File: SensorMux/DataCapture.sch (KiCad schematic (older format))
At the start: 0 parts

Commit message: Added byte start pulse generator
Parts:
- added C?: 220pF, symbol C
- added C?: C, symbol C
- added R?: 100, symbol R
- added R? (x2): 270, symbol R
- added U?: 74HC165, symbol 74LS165
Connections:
- new net: C?.2, R?.1
- new net: R?.1, U?.1 (Pl)
- new net +5V: C?.1, R?.1, U?.16 (VCC)
- new net CLK: U?.2 (CP)
- new net CLK_CNT_BIT_2: R?.2
- new net GND: C?.2, U?.15 (CE), U?.8 (GND)
- new net MISO: U?.9 (Q7)
- new net ~BYTE_START_PULSE: C?.1, R?.2, R?.2
- no-connect marks 0 -> 1
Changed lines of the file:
@@
 LIBS:contrib
 LIBS:valves
+LIBS:Trainiot
 LIBS:SensorMux-cache
 EELAYER 25 0
@@
 Comment4 ""
 $EndDescr
+Text HLabel 1350 4650 0    60   Input ~ 0
+CLK
+Wire Wire Line
+	1350 4650 8300 4650
+Text HLabel 1350 5900 0    60   Input ~ 0
+CLK_CNT_BUS
+Wire Bus Line
+	1350 5900 1850 5900
+Entry Wire Line
+	1550 5900 1650 6000
+Text Label 1700 6000 0    60   ~ 0
+CLK_CNT_BIT_2
+$Comp
+L C C?
+U 1 1 5A4D470C
+P 3250 6000
+F 0 "C?" H 3275 6100 50  0000 L CNN
+F 1 "220pF" H 3275 5900 50  0000 L CNN
+F 2 "" H 3288 5850 50  0001 C CNN
+F 3 "" H 3250 6000 50  0001 C CNN
+	1    3250 6000
+	0    1    1    0
+$EndComp
+Wire Wire Line
+	1650 6000 2650 6000
+$Comp
+L R R?
+U 1 1 5A4D4BAF
+P 2800 6000
+F 0 "R?" V 2880 6000 50  0000 C CNN
+F 1 "100" V 2800 6000 50  0000 C CNN
+F 2 "" V 2730 6000 50  0001 C CNN
+F 3 "" H 2800 6000 50  0001 C CNN
+	1    2800 6000
+	0    1    1    0
+$EndComp
+Wire Wire Line
+	3100 6000 2950 6000
+$Comp
+L R R?
+U 1 1 5A4D4C94
+P 3550 5600
+F 0 "R?" V 3630 5600 50  0000 C CNN
+F 1 "270" V 3550 5600 50  0000 C CNN
+F 2 "" V 3480 5600 50  0001 C CNN
+F 3 "" H 3550 5600 50  0001 C CNN
+	1    3550 5600
+	1    0    0    -1
+$EndComp
+Connection ~ 3550 6000
+Wire Wire Line
+	3550 6000 3550 5750
+Wire Wire Line
+	3550 5100 3550 5450
+Text Label 3850 6000 0    60   ~ 0
+~BYTE_START_PULSE
+$Comp
+L 74LS165 U?
+U 1 1 5A4D5180
+P 9000 4150
+F 0 "U?" H 9150 4100 50  0000 C CNN
+F 1 "74HC165" H 9150 3900 50  0000 C CNN
+F 2 "" H 9000 4150 50  0001 C CNN
+F 3 "" H 9000 4150 50  0001 C CNN
+	1    9000 4150
+	1    0    0    -1
+$EndComp
+$Comp
+L +5V #PWR?
+U 1 1 5A4D5497
+P 3550 5100
+F 0 "#PWR?" H 3550 4950 50  0001 C CNN
+F 1 "+5V" H 3550 5240 50  0000 C CNN
+F 2 "" H 3550 5100 50  0001 C CNN
+F 3 "" H 3550 5100 50  0001 C CNN
+	1    3550 5100
+	1    0    0    -1
+$EndComp
+Wire Wire Line
+	8300 4750 8200 4750
+Wire Wire Line
+	8200 4750 8200 4950
+$Comp
+L GND #PWR?
+U 1 1 5A4D54F4
+P 8700 5150
+F 0 "#PWR?" H 8700 4900 50  0001 C CNN
+F 1 "GND" H 8700 5000 50  0000 C CNN
+F 2 "" H 8700 5150 50  0001 C CNN
+F 3 "" H 8700 5150 50  0001 C CNN
+	1    8700 5150
+	1    0    0    -1
+$EndComp
+Wire Wire Line
+	8300 4500 7500 4500
+Wire Wire Line
+	7500 4500 7500 6000
+Wire Wire Line
+	9700 3650 10850 3650
+Text HLabel 10850 3650 2    60   Output ~ 0
+MISO
+NoConn ~ 9700 3750
+Wire Wire Line
+	8700 4800 8700 5150
+Wire Wire Line
+	8200 4950 8700 4950
+Connection ~ 8700 4950
+Wire Wire Line
+	8700 3500 8700 2700
+Wire Wire Line
+	8700 2700 8950 2700
+Wire Wire Line
+	8950 2550 8950 2800
+$Comp
+L +5V #PWR?
+U 1 1 5A4D5B17
+P 8950 2550
+F 0 "#PWR?" H 8950 2400 50  0001 C CNN
+F 1 "+5V" H 8950 2690 50  0000 C CNN
+F 2 "" H 8950 2550 50  0001 C CNN
+F 3 "" H 8950 2550 50  0001 C CNN
+	1    8950 2550
+	1    0    0    -1
+$EndComp
+Connection ~ 8950 2700
+$Comp
+L C C?
+U 1 1 5A4D5B79
+P 8950 2950
+F 0 "C?" H 8975 3050 50  0000 L CNN
+F 1 "C" H 8975 2850 50  0000 L CNN
+F 2 "" H 8988 2800 50  0001 C CNN
+F 3 "" H 8950 2950 50  0001 C CNN
+	1    8950 2950
+	1    0    0    -1
+$EndComp
+Wire Wire Line
+	8950 3100 8950 3200
+$Comp
+L GND #PWR?
+U 1 1 5A4D5C09
+P 8950 3200
+F 0 "#PWR?" H 8950 2950 50  0001 C CNN
+F 1 "GND" H 8950 3050 50  0000 C CNN
+F 2 "" H 8950 3200 50  0001 C CNN
+F 3 "" H 8950 3200 50  0001 C CNN
+	1    8950 3200
+	1    0    0    -1
+$EndComp
+$Comp
+L R R?
+U 1 1 5A4E7F3D
+P 5050 6000
+F 0 "R?" V 5130 6000 50  0000 C CNN
+F 1 "270" V 5050 6000 50  0000 C CNN
+F 2 "" V 4980 6000 50  0001 C CNN
+F 3 "" H 5050 6000 50  0001 C CNN
+	1    5050 6000
+	0    1    1    0
+$EndComp
+Wire Wire Line
+	7500 6000 5200 6000
+Wire Wire Line
+	3400 6000 4900 6000
 $EndSCHEMATC

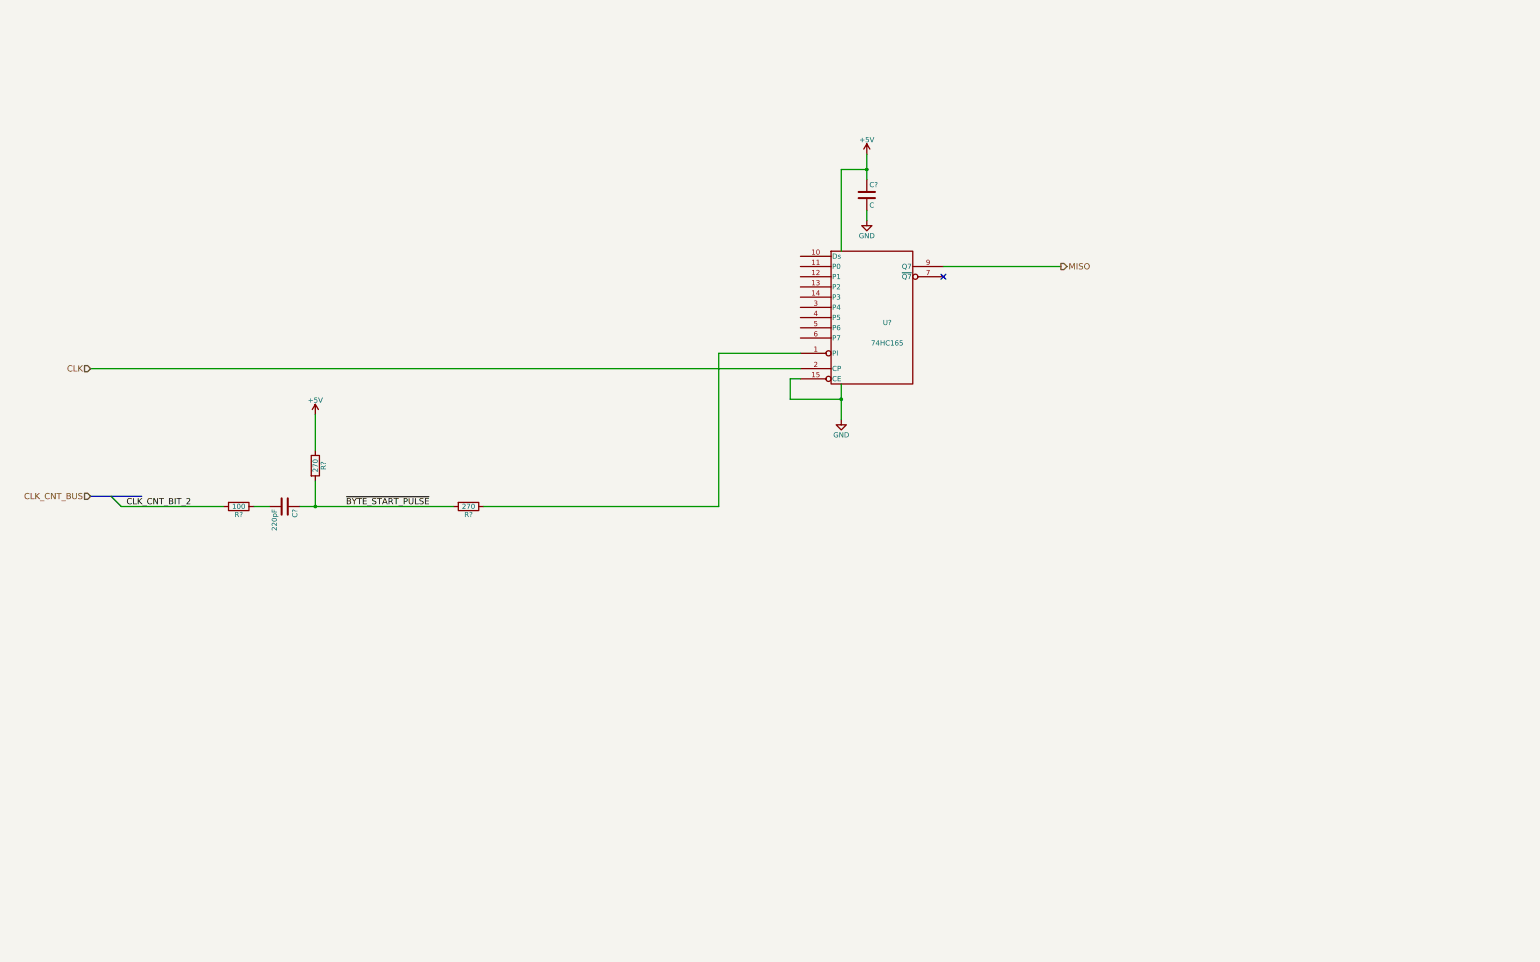
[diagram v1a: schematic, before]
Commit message: Added TLC5510 ADC with reference circuit on the power supply rails.
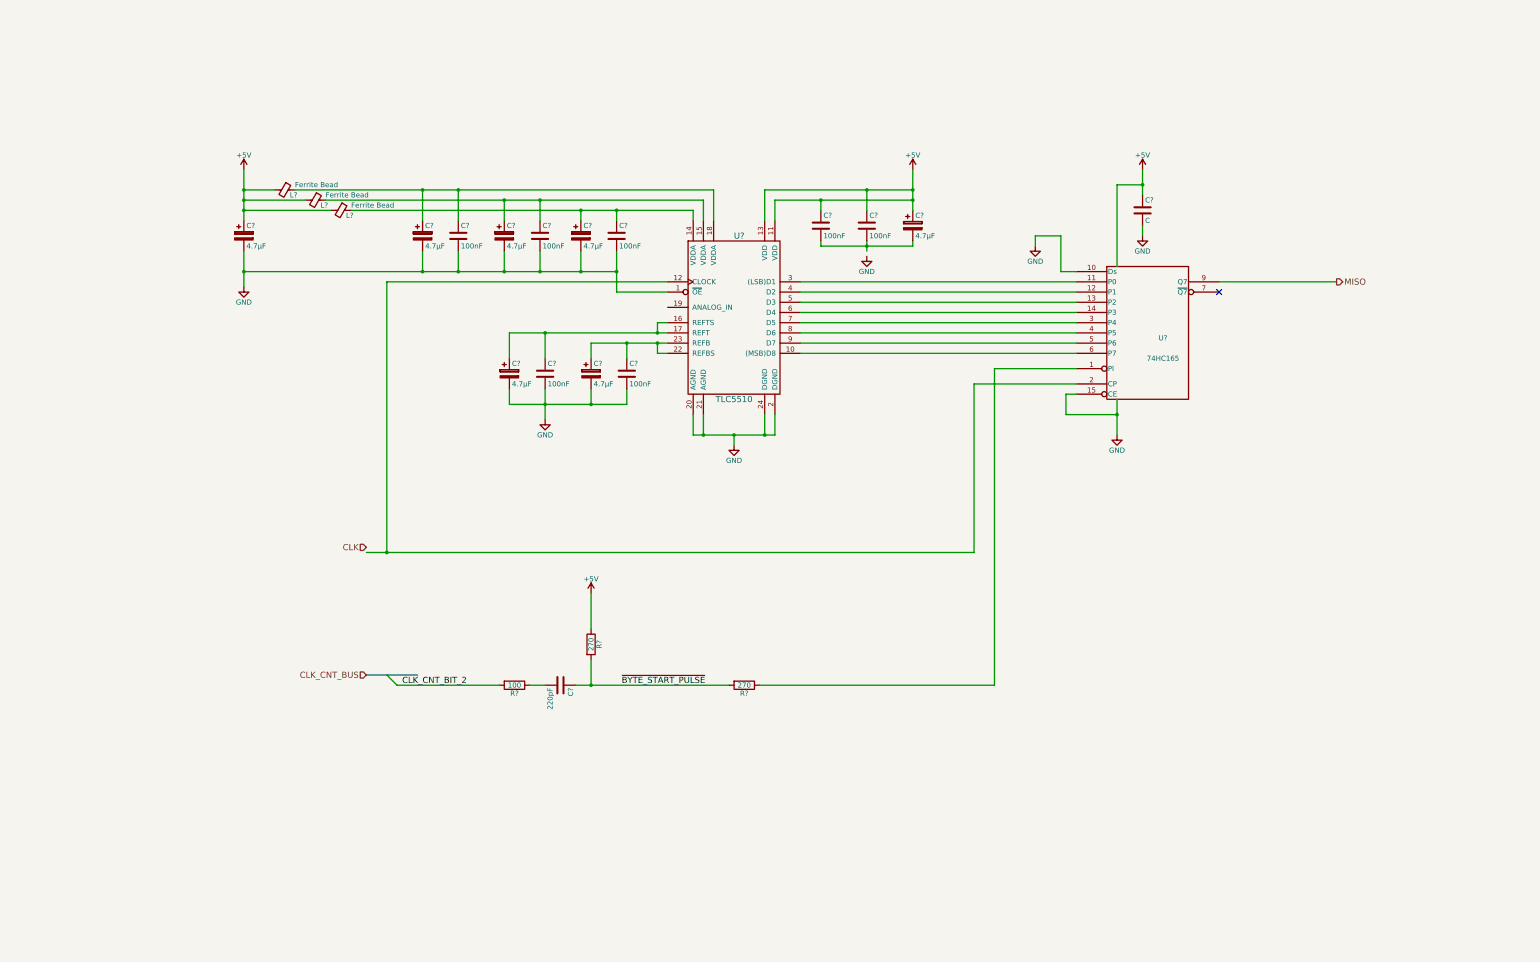
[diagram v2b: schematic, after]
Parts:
- added C? (x7): 100nF, symbol C
- added C? (x7): 4.7µF, symbol CP
- added L? (x3): Ferrite Bead, symbol Ferrite_Bead_Small
- added U?: TLC5510, symbol TLC5510
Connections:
- net +5V: now also C?.1, C?.1, C?.1, C?.1, L?.2, L?.2, L?.2, U?.11 (VDD), U?.13 (VDD)
- net CLK: no longer U?.2 (CP)
- net GND: now also U?.10 (Ds), C?.2, C?.2, C?.2, C?.2, C?.2, C?.2, C?.2, C?.2, C?.2, C?.2, C?.2, U?.1 (~OE), U?.2 (DGND), U?.20 (AGND), U?.21 (AGND), U?.24 (DGND)
- net at U?.11 (P0): now also U?.3 ((LSB)D1)
- net at U?.12 (P1): now also U?.4 (D2)
- net at U?.13 (P2): now also U?.5 (D3)
- net at U?.14 (P3): now also U?.6 (D4)
- net at U?.3 (P4): now also U?.7 (D5)
- net at U?.4 (P5): now also U?.8 (D6)
- net at U?.5 (P6): now also U?.9 (D7)
- net at U?.6 (P7): now also U?.10 ((MSB)D8)
- new net: U?.12 (CLOCK), U?.2 (CP)
- new net: C?.1, C?.1, L?.1, U?.14 (VDDA)
- new net: C?.1, C?.1, L?.1, U?.15 (VDDA)
- new net: C?.1, C?.1, U?.16 (REFTS), U?.17 (REFT)
- new net: C?.1, C?.1, L?.1, U?.18 (VDDA)
- new net: C?.1, C?.1, U?.22 (REFBS), U?.23 (REFB)
- new net: C?.2, C?.2, C?.2
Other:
- moved on the sheet: C?, R?, U?

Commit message: Working on adding analog part with SPI adjustment so the computer can control the opamps without needing manual trimpots.
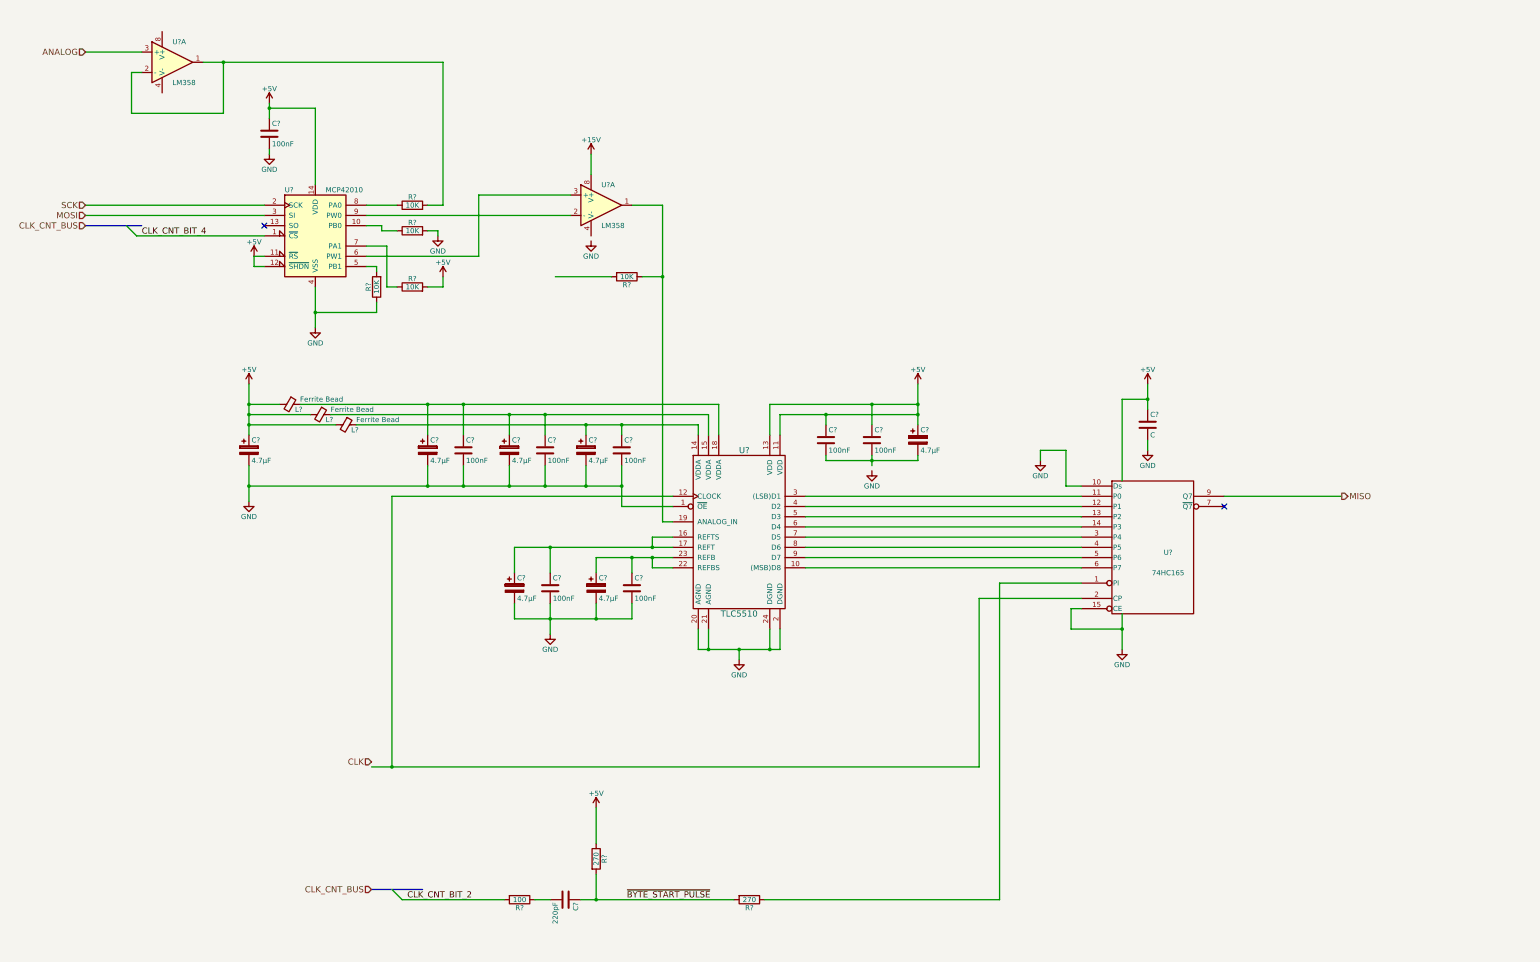
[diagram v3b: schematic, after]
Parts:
- added C?: 100nF, symbol C
- added R? (x5): 10K, symbol R
- added U? (x2): LM358, symbol LM358
- added U?: MCP42010, symbol MCP42010
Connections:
- net +5V: now also C?.1, R?.2, U?.11 (~RS), U?.12 (~SHDN), U?.14 (VDD)
- net GND: now also C?.2, R?.1, R?.2, U?.4 (VSS)
- net at U?.19 (ANALOG_IN): now also R?.1, U?.1
- new net: U?.2 (-), U?.9 (PW0)
- new net: U?.3 (+), U?.6 (PW1)
- new net: R?.2, U?.1, U?.2 (-)
- new net: R?.1, U?.10 (PB0)
- new net: R?.2, U?.5 (PB1)
- new net: R?.1, U?.7 (PA1)
- new net: R?.1, U?.8 (PA0)
- new net +15V: U?.8 (V+)
- new net ANALOG: U?.3 (+)
- new net CLK_CNT_BIT_4: U?.1 (~CS)
- new net MOSI: U?.3 (SI)
- new net SCK: U?.2 (SCK)
- no-connect marks 1 -> 2
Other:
- moved on the sheet: C?, L?, R?, U?

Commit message: Working on the analog input.
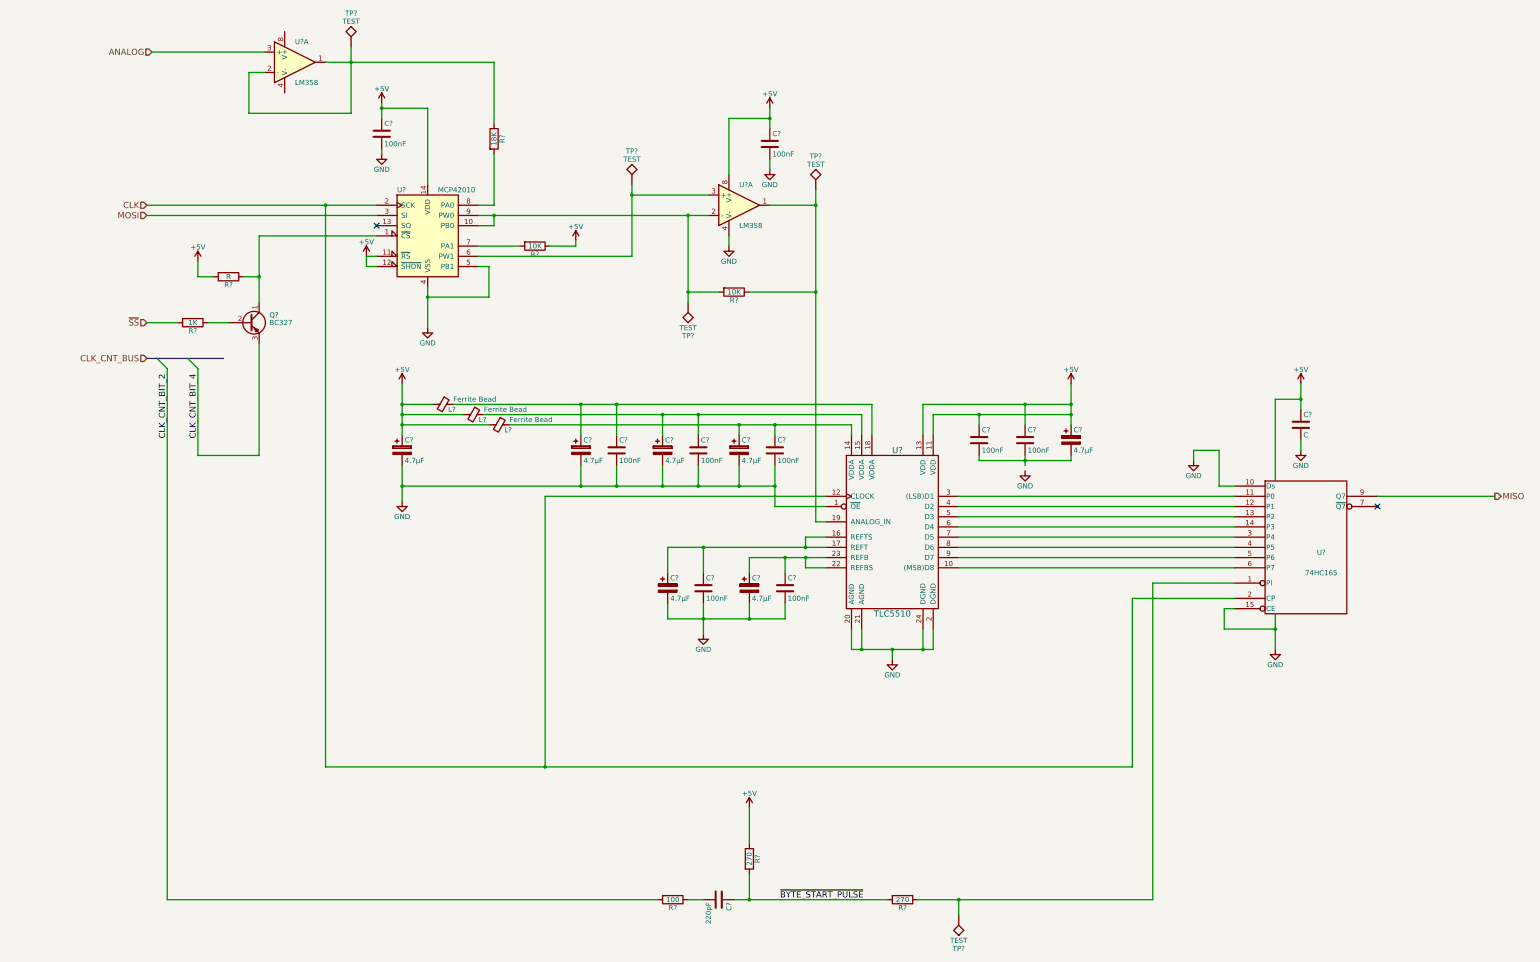
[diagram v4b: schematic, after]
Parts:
- removed R? (x5): 10K, symbol R
- added C?: 100nF, symbol C
- added Q?: BC327, TO_SOT_Packages_THT:TO-92_Molded_Narrow, symbol BC327
- added R? (x2): 10K, symbol R
- added R?: 18K, symbol R
- added R?: 1K, symbol R
- added R?: R, symbol R
- added TP? (x5): TEST, symbol TEST
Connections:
- net +15V is gone; now on net +5V: U?.8 (V+)
- net SCK is gone; now on net CLK: U?.2 (SCK)
- net +5V: now also C?.1, R?.1, R?.2
- net CLK: now also U?.12 (CLOCK), U?.2 (CP)
- net CLK_CNT_BIT_4: now also Q?.3 (E); no longer U?.1 (~CS)
- net GND: now also U?.4 (V-), U?.5 (PB1), C?.2
- net at R?.1, U?.1 (Pl): now also TP?.1
- net at U?.1, U?.19 (ANALOG_IN): now also R?.1, TP?.1
- net at U?.2 (-), U?.9 (PW0): now also U?.10 (PB0), R?.2, TP?.1
- net at U?.3 (+), U?.6 (PW1): now also TP?.1
- net at U?.1, U?.2 (-): now also R?.1, TP?.1
- net at U?.7 (PA1): now also R?.2
- net at U?.8 (PA0): now also R?.2
- new net: Q?.1 (C), R?.1, U?.1 (~CS)
- new net: Q?.2 (B), R?.1
- new net ~SS: R?.2
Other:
- moved on the sheet: C?, L?, R?, U?, U?A
